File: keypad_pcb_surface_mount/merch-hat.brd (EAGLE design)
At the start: 65 x 56 mm, 15 parts

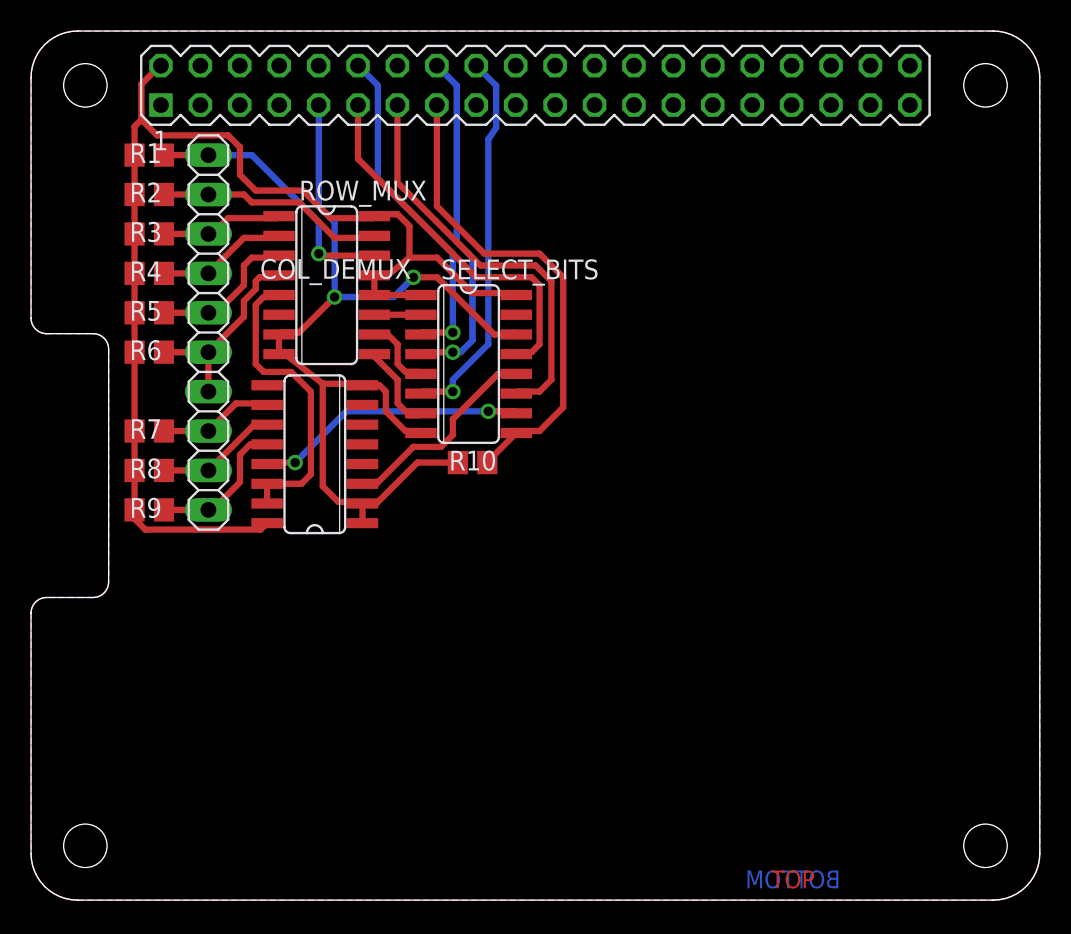
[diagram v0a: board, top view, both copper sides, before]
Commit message: Move Keypad, Add Port Sensor
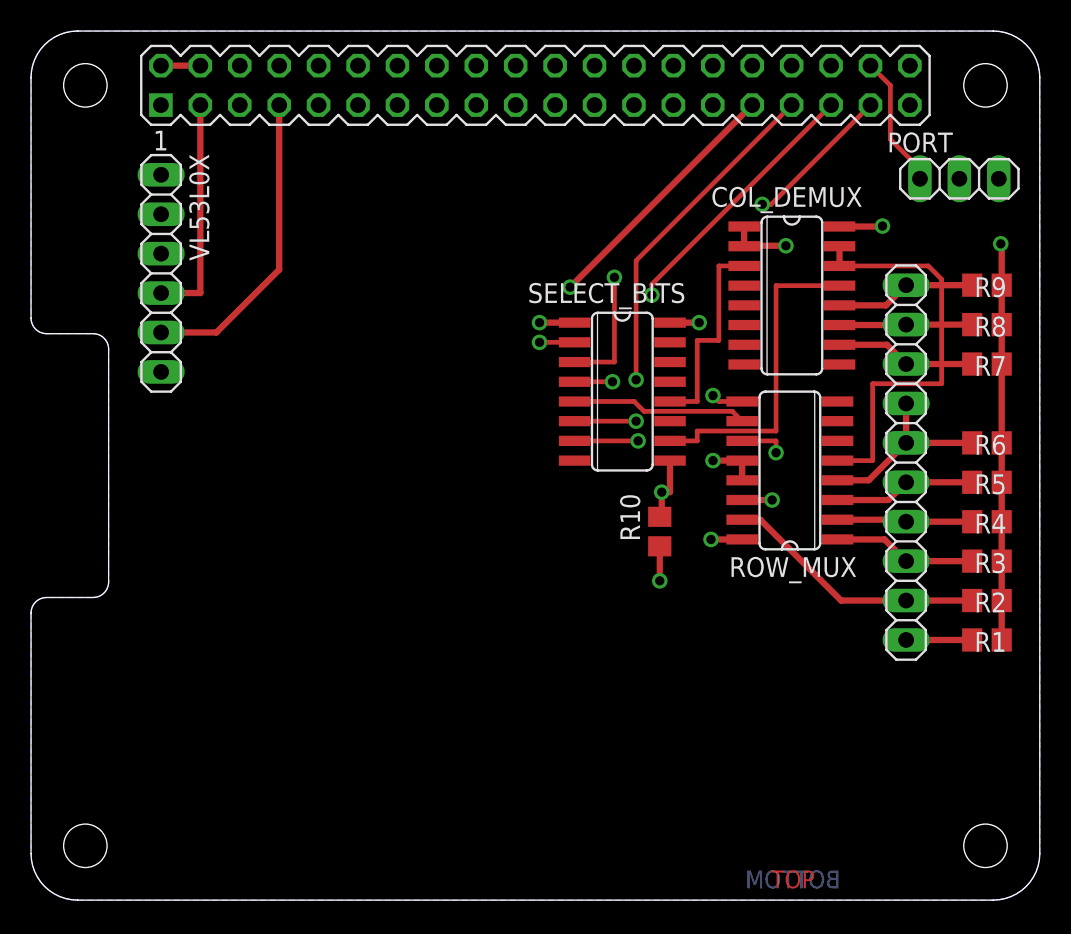
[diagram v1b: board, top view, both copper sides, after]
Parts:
- removed JP1: HEADER, pinhead:1X10
- added KEYPAD: KEYPAD, pinhead:1X10
- added PORT: Sensor Port, pinhead:1X03
- added VL53L0X: VL53L0X, pinhead:1X06
- moved R1 62.4 mm to (61.6, 16.8), turned to 180 degrees
- moved R2 60.0 mm to (61.6, 19.3), turned to 180 degrees
- moved R3 57.9 mm to (61.6, 21.8), turned to 180 degrees
- moved R4 56.3 mm to (61.6, 24.4), turned to 180 degrees
- moved R9 55.9 mm to (61.6, 39.6), turned to 180 degrees
- moved R5 55.1 mm to (61.6, 26.9), turned to 180 degrees
- moved R8 54.8 mm to (61.6, 37.1), turned to 180 degrees
- moved R6 54.3 mm to (61.6, 29.5), turned to 180 degrees
- moved R7 54.1 mm to (61.6, 34.5), turned to 180 degrees
- moved COL_DEMUX 32.4 mm to (49.0, 39.0), turned to 270 degrees
- moved ROW_MUX 32.1 mm to (48.9, 27.7), turned to 90 degrees
- moved R10 12.9 mm to (40.5, 23.7), turned to 90 degrees
- moved SELECT_BITS 10.1 mm to (38.1, 32.8)
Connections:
- removed net N$7: GPIO.11, SELECT_BITS.13
- removed net N$8: GPIO.15, R10.2, SELECT_BITS.9
- new net 3.3V: GPIO.1
- new net 5V: COL_DEMUX.8, ROW_MUX.8, SELECT_BITS.14, SELECT_BITS.8
- new net CLK: GPIO.31, R10.2, SELECT_BITS.9
- new net N$19: GPIO.5, VL53L0X.3
- new net N$23: GPIO.3, VL53L0X.4
- new net N$24: GPIO.7, VL53L0X.5
- net +5V: now also GPIO.4, VL53L0X.1
- net GND: now also GPIO.39, GPIO.40, PORT.3, VL53L0X.2; no longer COL_DEMUX.8, GPIO.9, ROW_MUX.8, SELECT_BITS.14, SELECT_BITS.8
- net N$1: now also KEYPAD.1; no longer JP1.1
- net N$10: now also KEYPAD.4; no longer JP1.4
- net N$11: now also KEYPAD.5; no longer JP1.5
- net N$13: now also KEYPAD.6, KEYPAD.7; no longer JP1.6, JP1.7
- net N$14: now also KEYPAD.8; no longer JP1.8
- net N$15: now also KEYPAD.9; no longer JP1.9
- net N$16: now also KEYPAD.10; no longer JP1.10
- net N$2: now also GPIO.33, SELECT_BITS.6; no longer GPIO.16, SELECT_BITS.4
- net N$3: now also GPIO.35, SELECT_BITS.4; no longer GPIO.18, SELECT_BITS.6
- net N$4: now also KEYPAD.2; no longer JP1.2
- net N$5: now also GPIO.37, SELECT_BITS.3; no longer GPIO.13, SELECT_BITS.11
- net N$6: now also GPIO.38, PORT.1; no longer GPIO.12, SELECT_BITS.3
- net N$9: now also KEYPAD.3; no longer JP1.3
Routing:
- net GND: track 62.7 -> 6.22 mm
- net CLK: track 0.00 -> 46.2 mm, vias 0 -> 2
- net +5V: track 77.3 -> 40.4 mm, vias 0 -> 6
- net N$8: track 31.3 -> 0.00 mm
- net N$12: track 3.00 -> 29.1 mm, vias 0 -> 2
- net N$7: track 24.1 -> 0.00 mm
- net N$24: track 0.00 -> 19.9 mm
- net N$23: track 0.00 -> 14.6 mm
- net N$19: track 0.00 -> 14.6 mm
- net N$6: track 21.8 -> 8.61 mm, vias 1 -> 0
- net N$18: track 5.66 -> 13.4 mm, vias 0 -> 2
- net N$22: track 19.5 -> 26.6 mm
- net N$17: track 4.79 -> 11.3 mm
- net N$2: track 22.3 -> 28.5 mm, vias 1 -> 2
- net N$20: track 17.5 -> 20.9 mm, vias 2 -> 0
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- added copper zone on layer 15, net +5V
- removed copper zone on layer 1, net GND

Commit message: Finish Up Surface Mount Version
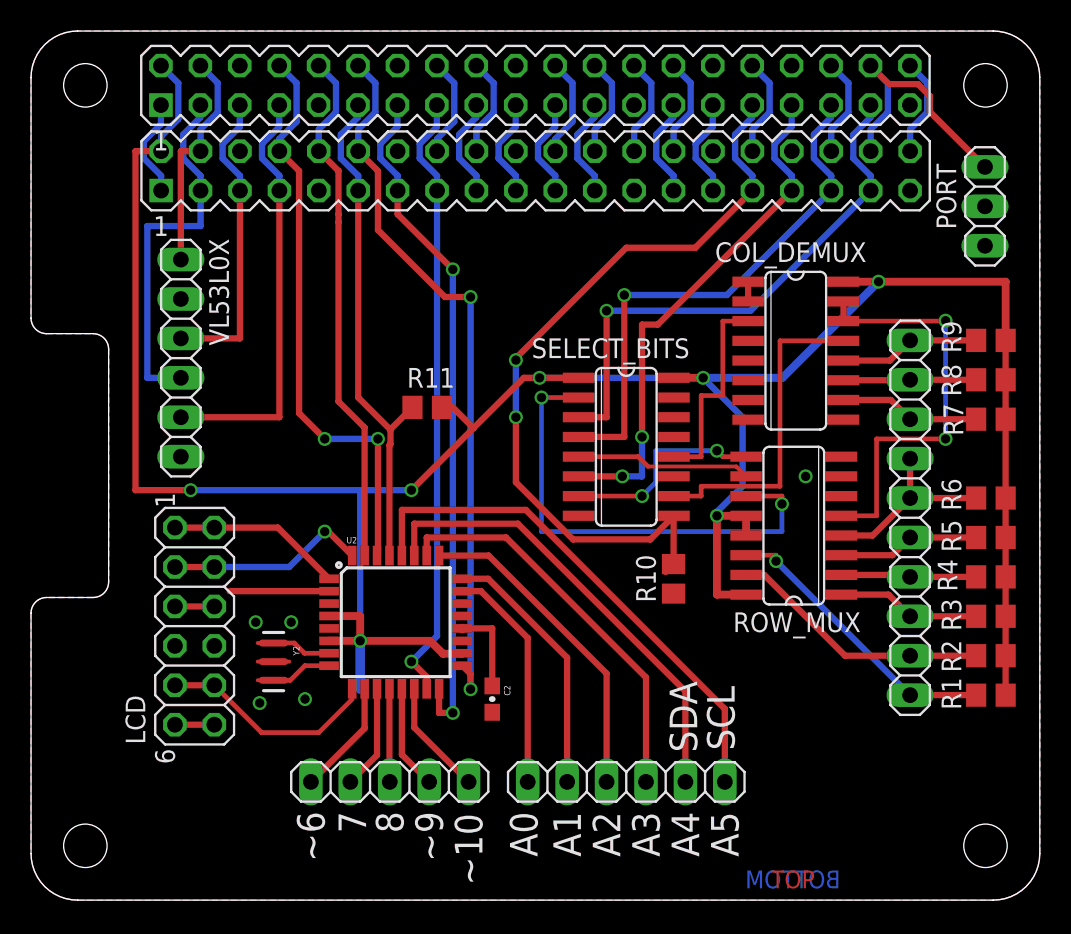
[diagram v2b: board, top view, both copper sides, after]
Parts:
- added C2: 0.1uF, SparkFun-Capacitors:0603-CAP
- added GPIO1: PIN20X2, FLYFISH:PIN_20X2
- added JP1: (no value), pinhead:1X06
- added JP3: (no value), pinhead:1X05
- added LCD: (no value), pinhead:2X06
- added R11: 3.3k, resistor:R0805
- added U2: ATMEGA328P_TQFP, SparkFun-DigitalIC:TQFP32-08
- added Y2: 16MHZ, SparkFun-FreqCtrl:RESONATOR-SMD
- moved VL53L0X 5.61 mm to (9.65, 34.9)
- moved COL_DEMUX 3.57 mm to (49.3, 35.4)
- moved R8 3.57 mm to (61.8, 33.5)
- moved R9 3.57 mm to (61.8, 36.1)
- moved R3 3.57 mm to (61.8, 18.3)
- moved R4 3.57 mm to (61.8, 20.8)
- moved R5 3.57 mm to (61.8, 23.4)
- moved ROW_MUX 3.57 mm to (49.1, 24.1)
- moved R1 3.57 mm to (61.8, 13.2)
- moved R2 3.57 mm to (61.8, 15.7)
- moved KEYPAD 3.57 mm to (56.6, 24.6)
- moved R6 3.57 mm to (61.8, 25.9)
- moved R7 3.57 mm to (61.8, 31.0)
- moved SELECT_BITS 3.57 mm to (38.4, 29.2)
- moved R10 3.17 mm to (41.4, 20.7)
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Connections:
- removed net 5V: COL_DEMUX.8, ROW_MUX.8, SELECT_BITS.14, SELECT_BITS.8
- removed net CLK: GPIO.31, R10.2, SELECT_BITS.9
- removed net N$19: GPIO.5, VL53L0X.3
- removed net N$2: GPIO.33, SELECT_BITS.6
- removed net N$23: GPIO.3, VL53L0X.4
- removed net N$24: GPIO.7, VL53L0X.5
- removed net N$3: GPIO.35, SELECT_BITS.4
- removed net N$5: GPIO.37, SELECT_BITS.3
- removed net N$6: GPIO.38, PORT.1
- new net /RESET: LCD.11, LCD.12, U2.1
- new net AD0: JP1.1, U2.23
- new net AD1: JP1.2, U2.24
- new net AD2: JP1.3, U2.25
- new net AD3: JP1.4, U2.26
- new net AD4/SDA: JP1.5, U2.27
- new net AD5/SCL: JP1.6, U2.28
- new net BUSY: LCD.7, LCD.8, U2.2
- new net GPIO10: GPIO.19, GPIO1.19
- new net GPIO11: GPIO.23, GPIO1.23
- new net GPIO12: GPIO.32, GPIO1.32
- new net GPIO13: GPIO.33, GPIO1.33, SELECT_BITS.6
- new net GPIO16: GPIO.36, GPIO1.36
- new net GPIO19: GPIO.35, GPIO1.35, SELECT_BITS.4
- new net GPIO2: GPIO.3, GPIO1.3, VL53L0X.4
- new net GPIO20: GPIO.38, GPIO1.38, PORT.1
- new net GPIO21: GPIO.40, GPIO1.40
- new net GPIO23: GPIO.16, GPIO1.16
- new net GPIO24: GPIO.18, GPIO1.18
- new net GPIO25: GPIO.22, GPIO1.22
- new net GPIO26: GPIO.37, GPIO1.37, SELECT_BITS.3
- new net GPIO3: GPIO.5, GPIO1.5, VL53L0X.3
- new net GPIO4: GPIO.7, GPIO1.7, VL53L0X.5
- new net GPIO5: GPIO.29, GPIO1.29
- new net GPIO6: GPIO.31, GPIO1.31, R10.2, SELECT_BITS.9
- new net GPIO7: GPIO.26, GPIO1.26
- new net GPIO8: GPIO.24, GPIO1.24
- new net GPIO9: GPIO.21, GPIO1.21
- new net ICSP_MISO: GPIO.13, GPIO1.13, U2.16
- new net ICSP_MOSI: GPIO.15, GPIO1.15, U2.15
- new net ICSP_RESET: GPIO.11, GPIO1.11, R11.2, U2.29
- new net ICSP_SCK: GPIO.12, GPIO1.12, U2.17
- new net ID_SC: GPIO.28, GPIO1.28
- new net ID_SD: GPIO.27, GPIO1.27
- new net IO10/SS: JP3.5, U2.14
- new net IO6: JP3.1, U2.10
- new net IO7: JP3.2, U2.11
- new net IO8: JP3.3, U2.12
- new net IO9: JP3.4, U2.13
- new net N$29: U2.7, Y2.1
- new net N$30: U2.8, Y2.3
- new net N$32: C2.1, U2.20
- new net PI_RXD: GPIO.10, GPIO1.10, U2.31
- new net PI_TXD: GPIO.8, GPIO1.8, U2.30
- new net SCK: LCD.10, LCD.9, U2.32
- new net SIN: LCD.3, LCD.4, U2.9
- new net VCC: LCD.1, LCD.2
- net +5V: now also GPIO1.2, GPIO1.4, R11.1, U2.18, U2.4, U2.6
- net 3.3V: now also GPIO.17, GPIO1.1, GPIO1.17
- net GND: now also C2.2, COL_DEMUX.8, GPIO.14, GPIO.20, GPIO.25, GPIO.30, GPIO.34, GPIO.6, GPIO.9, GPIO1.14, GPIO1.20, GPIO1.25, GPIO1.30, GPIO1.34, GPIO1.39, GPIO1.6, GPIO1.9, LCD.5, LCD.6, ROW_MUX.8, SELECT_BITS.14, SELECT_BITS.8, U2.21, U2.3, U2.5, Y2.2; no longer GPIO.40
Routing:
- net +5V: track 40.4 -> 188.2 mm, vias 6 -> 7
- net GPIO6: track 0.00 -> 50.3 mm, vias 0 -> 2
- net ICSP_SCK: track 0.00 -> 46.8 mm, vias 0 -> 2
- net CLK: track 46.2 -> 0.00 mm, vias 2 -> 0
- net ICSP_MISO: track 0.00 -> 44.0 mm, vias 0 -> 2
- net ICSP_MOSI: track 0.00 -> 39.6 mm, vias 0 -> 1
- net PI_TXD: track 0.00 -> 37.2 mm, vias 0 -> 2
- net GPIO26: track 0.00 -> 35.3 mm, vias 0 -> 1
- net GPIO19: track 0.00 -> 34.6 mm, vias 0 -> 1
- net AD5/SCL: track 0.00 -> 33.8 mm
- net PI_RXD: track 0.00 -> 33.7 mm
- net GPIO13: track 0.00 -> 33.5 mm, vias 0 -> 2
- net ICSP_RESET: track 0.00 -> 32.9 mm
- net AD4/SDA: track 0.00 -> 29.8 mm
- net N$5: track 29.2 -> 0.00 mm, vias 2 -> 0
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- added copper zone on layer 1, net GND
- removed copper zone on layer 15, net +5V
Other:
- board text added: "7"
- board text added: "8"
- board text added: "A0"
- board text added: "A1"
- board text added: "A2"
- board text added: "A3"
- board text added: "A4"
- board text added: "A5"
- board text added: "SCL"
- board text added: "SDA"
- board text added: "~10"
- board text added: "~6"
- board text added: "~9"

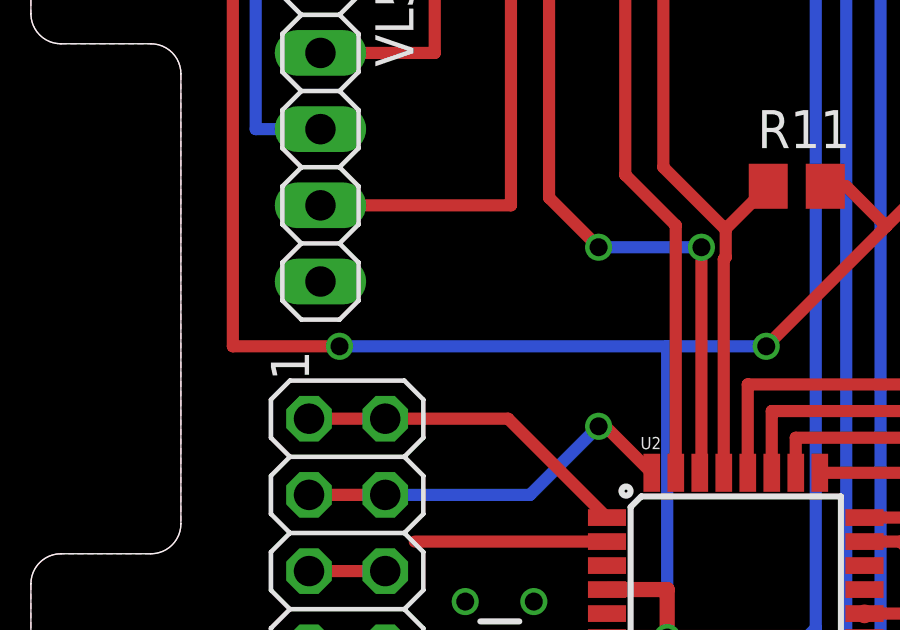
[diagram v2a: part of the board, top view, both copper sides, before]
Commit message: add decoupling cap
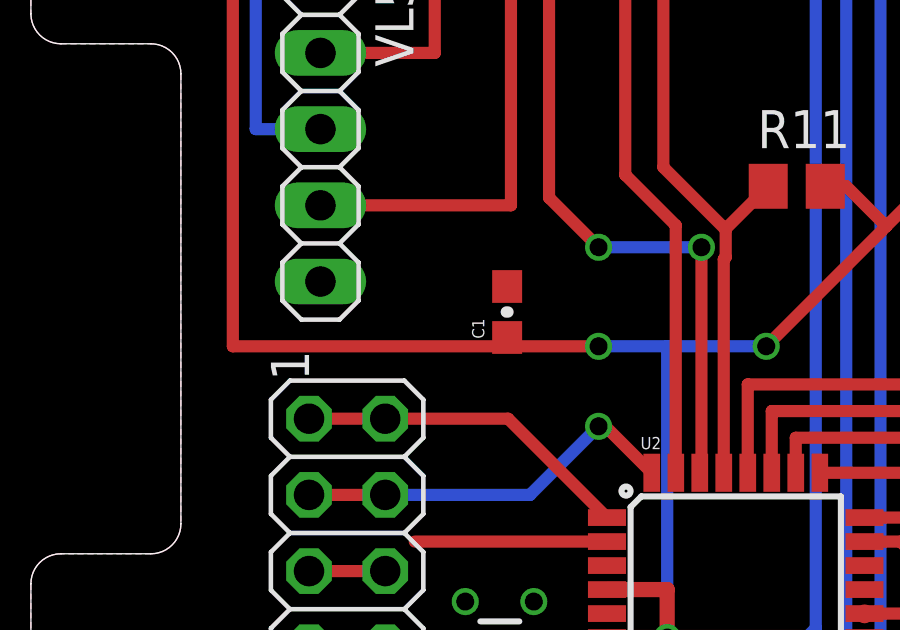
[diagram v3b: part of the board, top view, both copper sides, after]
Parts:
- added C1: 0.1uF, SparkFun-Capacitors:0603-CAP
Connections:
- net +5V: now also C1.1
- net GND: now also C1.2
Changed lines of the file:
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@@
 <?xml version="1.0" encoding="utf-8"?>
 <!DOCTYPE eagle SYSTEM "eagle.dtd">
-<eagle version="8.1.0">
+<eagle version="8.0.1">
 <drawing>
 <settings>
@@
 <attribute name="VALUE" x="26.162" y="34.29" size="1.27" layer="27" rot="R180"/>
 </element>
+<element name="C1" library="SparkFun-Capacitors" package="0603-CAP" value="0.1uF" x="15.875" y="27.559" rot="R90"/>
 </elements>
 <signals>
@@
 <wire x1="8.382" y1="48.26" x2="6.731" y2="48.26" width="0.4064" layer="1"/>
 <wire x1="6.731" y1="48.26" x2="6.731" y2="26.416" width="0.4064" layer="1"/>
-<wire x1="6.731" y1="26.416" x2="10.287" y2="26.416" width="0.4064" layer="1"/>
-<via x="10.287" y="26.416" extent="1-16" drill="0.6"/>
-<wire x1="10.287" y1="26.416" x2="21.209" y2="26.416" width="0.4064" layer="16"/>
+<wire x1="15.875" y1="26.416" x2="6.731" y2="26.416" width="0.4064" layer="1"/>
+<via x="18.923" y="26.416" extent="1-16" drill="0.6"/>
+<wire x1="15.875" y1="26.416" x2="18.923" y2="26.416" width="0.4064" layer="1"/>
+<wire x1="18.923" y1="26.416" x2="21.209" y2="26.416" width="0.4064" layer="16"/>
 <wire x1="21.209" y1="26.416" x2="21.209" y2="16.707" width="0.4064" layer="16"/>
 <wire x1="21.209" y1="26.416" x2="24.511" y2="26.416" width="0.4064" layer="16"/>
@@
 <wire x1="26.477" y1="31.75" x2="27.178" y2="31.75" width="0.4064" layer="1"/>
 <wire x1="27.178" y1="31.75" x2="28.5115" y2="30.4165" width="0.4064" layer="1"/>
+<contactref element="C1" pad="1"/>
+<wire x1="15.875" y1="26.709" x2="15.875" y2="26.416" width="0.4064" layer="1"/>
 <wire x1="8.382" y1="48.26" x2="9.652" y2="48.26" width="0" layer="19" extent="1-16"/>
 </signal>
@@
 <contactref element="GPIO1" pad="30"/>
 <contactref element="GPIO1" pad="34"/>
+<contactref element="C1" pad="2"/>
 </signal>
 <signal name="GPIO20">
